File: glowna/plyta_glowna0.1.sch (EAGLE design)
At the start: 217 parts, among them IC1 4504D, IC2 MAX481CSA, IC3 4504D, IC4 OPA4658UU, Q1 CSM-7X-DU, Q2 N-HEXFET-2D_SOT232-IRLL014N, Q3 N-HEXFET-2D_SOT232-IRLL014N, Q4 N-HEXFET-2D_SOT232-IRLL014N, Q5 N-HEXFET-2D_SOT232-IRLL014N, Q6 N-HEXFET-2D_SOT232-IRLL014N, X1 MINI-USB_SHIELD5P2-32005-601

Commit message: a
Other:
- note removed: "może jakiś elektrolit ?"
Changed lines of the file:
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@@
 <?xml version="1.0" encoding="utf-8"?>
 <!DOCTYPE eagle SYSTEM "eagle.dtd">
-<eagle version="7.5.0">
+<eagle version="7.2.0">
 <drawing>
 <settings>
@@
 <text x="-43.18" y="91.44" size="5.08" layer="99">Jaki
 kwarc?</text>
-<text x="-139.7" y="71.12" size="1.27" layer="99">może jakiś elektrolit ?</text>
 <text x="157.48" y="-17.78" size="6.4516" layer="97">USB</text>
 <wire x1="434.34" y1="91.44" x2="500.38" y2="91.44" width="0.1524" layer="97" style="longdash"/>

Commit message: konczymy
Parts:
- added R65, R66, R67: (no value), rcl:R-EU_R2512
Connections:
- net N$77 renamed W1_1
- net N$83 renamed W2_1
- net N$85 renamed W3_1
- removed net N$78: R50.1
- removed net N$84: R58.1
- removed net N$86: R61.1
- new net W1_2: R50.1, R65.1, U$7.P$1, U$7.P$2
- new net W2_2: R58.1, R66.1, U$9.P$1, U$9.P$2
- new net W3_2: R61.1, R67.1, U$11.P$1, U$11.P$2
- net +24V: now also R65.2, R66.2, R67.2; no longer U$11.P$1, U$11.P$2, U$7.P$1, U$7.P$2, U$9.P$1, U$9.P$2
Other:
- note added: "może jakiś elektrolit ?"

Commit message: koniec?
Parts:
- added U$20, U$21, U$22: SEPARATOR, robione:SEPARATOR
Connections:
- net +24V: now also U$20.1, U$21.1, U$22.1
- net W1_1: now also U$20.2
- net W2_1: now also U$21.2
- net W3_1: now also U$22.2
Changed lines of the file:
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@@
 <part name="P+5" library="supply1" deviceset="+24V" device=""/>
 <part name="P+6" library="supply1" deviceset="+24V" device=""/>
+<part name="U$20" library="robione" deviceset="SEPARATOR" device=""/>
+<part name="U$21" library="robione" deviceset="SEPARATOR" device=""/>
+<part name="U$22" library="robione" deviceset="SEPARATOR" device=""/>
 </parts>
 <sheets>
@@
 <attribute name="VALUE" x="220.98" y="76.2" size="1.778" layer="96" rot="R180"/>
 </instance>
+<instance part="U$20" gate="G$1" x="226.06" y="119.38"/>
+<instance part="U$21" gate="G$1" x="223.52" y="93.98"/>
+<instance part="U$22" gate="G$1" x="223.52" y="68.58"/>
 </instances>
 <busses>
@@
 <wire x1="220.98" y1="119.38" x2="223.52" y2="119.38" width="0.1524" layer="91"/>
 <junction x="220.98" y="119.38"/>
+<pinref part="U$20" gate="G$1" pin="1"/>
 </segment>
 <segment>
@@
 <wire x1="220.98" y1="96.52" x2="220.98" y2="93.98" width="0.1524" layer="91"/>
 <pinref part="P+5" gate="1" pin="+24V"/>
-<wire x1="220.98" y1="93.98" x2="223.52" y2="93.98" width="0.1524" layer="91"/>
+<pinref part="U$21" gate="G$1" pin="1"/>
 <junction x="220.98" y="93.98"/>
-<label x="223.52" y="93.98" size="1.778" layer="95" xref="yes"/>
 </segment>
 <segment>
@@
 <wire x1="220.98" y1="68.58" x2="220.98" y2="71.12" width="0.1524" layer="91"/>
 <pinref part="P+6" gate="1" pin="+24V"/>
-<wire x1="220.98" y1="68.58" x2="223.52" y2="68.58" width="0.1524" layer="91"/>
+<pinref part="U$22" gate="G$1" pin="1"/>
 <junction x="220.98" y="68.58"/>
-<label x="223.52" y="68.58" size="1.778" layer="95" xref="yes"/>
 </segment>
 </net>
@@
 <label x="-170.18" y="2.54" size="1.6764" layer="95" rot="R180" xref="yes"/>
 </segment>
+<segment>
+<pinref part="U$20" gate="G$1" pin="2"/>
+<wire x1="228.6" y1="119.38" x2="231.14" y2="119.38" width="0.1524" layer="91"/>
+<label x="231.14" y="119.38" size="1.27" layer="95" xref="yes"/>
+</segment>
 </net>
 <net name="W1_2" class="0">
@@
 <label x="-177.8" y="-27.94" size="1.6764" layer="95" rot="R180" xref="yes"/>
 </segment>
+<segment>
+<pinref part="U$21" gate="G$1" pin="2"/>
+<wire x1="226.06" y1="93.98" x2="228.6" y2="93.98" width="0.1524" layer="91"/>
+<label x="228.6" y="93.98" size="1.27" layer="95" xref="yes"/>
+</segment>
 </net>
 <net name="W2_2" class="0">
@@
 <label x="-101.6" y="2.54" size="1.6764" layer="95" rot="R180" xref="yes"/>
 </segment>
+<segment>
+<pinref part="U$22" gate="G$1" pin="2"/>
+<wire x1="226.06" y1="68.58" x2="228.6" y2="68.58" width="0.1524" layer="91"/>
+<label x="228.6" y="68.58" size="1.27" layer="95" xref="yes"/>
+</segment>
 </net>

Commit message: to juz jest koniec
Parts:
- added U$23, U$24, U$25: SEPARATOR, robione:SEPARATOR
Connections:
- new net N$77: R65.2, U$23.2, U$8.P$1, U$8.P$2
- new net N$78: R66.1, U$10.P$1, U$10.P$2, U$24.2
- new net N$83: R67.1, U$12.P$1, U$12.P$2, U$25.2
- net +24V: now also U$11.P$1, U$11.P$2, U$7.P$1, U$7.P$2, U$9.P$1, U$9.P$2; no longer R65.2, R66.2, R67.2, U$20.1, U$21.1, U$22.1
- net GND: now also R65.1, R66.2, R67.2, U$20.1, U$21.1, U$22.1; no longer U$10.P$1, U$10.P$2, U$12.P$1, U$12.P$2, U$8.P$1, U$8.P$2
- net W1_1: now also U$23.1; no longer U$20.2
- net W1_2: now also U$20.2; no longer R65.1, U$7.P$1, U$7.P$2
- net W2_1: now also U$24.1; no longer U$21.2
- net W2_2: now also U$21.2; no longer R66.1, U$9.P$1, U$9.P$2
- net W3_1: now also U$25.1; no longer U$22.2
- net W3_2: now also U$22.2; no longer R67.1, U$11.P$1, U$11.P$2
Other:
- moved on the sheet: R65, R66, R67

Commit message: z mojej strony koniec
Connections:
- removed net GPIO_WENTYLATOR: U$1.PG2
- removed net N$22: IC1A.AI
- removed net N$23: JP25.3
- removed net N$24: JP25.2
- removed net N$25: IC1A.BI
- removed net N$27: JP26.1
- removed net N$28: IC1A.CI
- removed net N$29: JP26.8
- removed net N$30: IC1A.DI
- removed net N$31: IC1A.EI
- removed net N$32: IC1A.FI
- removed net TIM4_PWM_WENTYLATOR: U$1.PD15
- new net GPIO_WEN: IC1A.FI, U$1.PG2
- new net TIM4_PWM_WEN: IC1A.EI, U$1.PD15
- new net VDD: C22.+, D_1.C, D_2.C, D_3.C, D_4.C, F2.2, GRZALKA.2, GRZALKA1.2, GRZALKA2.2, GRZALKA3.2, TRANSIL_3.C
- net +24V: no longer C22.+, D_1.C, D_2.C, D_3.C, D_4.C, F2.2, GRZALKA.2, GRZALKA1.2, GRZALKA2.2, GRZALKA3.2, TRANSIL_3.C
- net GND: no longer JP26.6
- net GRZALKA1: now also IC1A.AI
- net GRZALKA2: now also IC1A.BI
- net GRZALKA3: now also IC1A.CI
- net GRZALKA4: now also IC1A.DI
- net I2C1_SCL: now also JP25.2
- net I2C1_SDA: now also JP25.3
- net UART4_WIFI_RX: now also JP26.1
- net UART4_WIFI_TX: now also JP26.8
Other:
- note added: "Odcinanie sterownika 12v"
- note added: "Pomiar pradu"
- note removed: "Miso & mosi dla pewności do sprawdzenia"
- moved on the sheet: C28

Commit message: zabezpieczenia
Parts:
- added D27, D28, D29, D30, D31, D32, D33, D34, D35, D36, D37, D38, D39: BAT54S, diode:BAT54S
- added R68, R69, R70, R71, R72, R73, R74, R75, R76, R77, R78, R79, R80: 5k, rcl:R-EU_R0603
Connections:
- new net N$22: D28.C1A2, JP17.1, R69.2
- new net N$23: JP7.1, R68.2
- new net N$24: D32.C1A2, JP19.1, R71.2
- new net N$25: D33.C1A2, JP18.1, R70.2
- new net N$27: D31.C1A2, JP20.1, R72.2
- new net N$28: D30.C1A2, JP22.1, R74.2
- new net N$29: D29.C1A2, JP21.1, R73.2
- new net N$32: JP24.1, R75.1
- new net N$84: JP24.3, R76.1
- new net N$85: JP24.5, R77.1
- new net N$86: JP24.7, R78.1
- new net N$87: JP24.9, R79.1
- new net N$88: JP24.11, R80.1
- net +3V3: now also D27.C2, D28.C2, D29.C2, D30.C2, D31.C2, D32.C2, D33.C2, D34.C2, D35.C2, D36.C2, D37.C2, D38.C2, D39.C2
- net ENDSTOP1: now also D36.C1A2, R78.2; no longer JP24.7
- net ENDSTOP2: now also D35.C1A2, R79.2; no longer JP24.9
- net ENDSTOP3: now also D34.C1A2, R80.2; no longer JP24.11
- net ENDSTOP_E1: now also D39.C1A2, R75.2; no longer JP24.1
- net ENDSTOP_E2: now also D38.C1A2, R76.2; no longer JP24.3
- net ENDSTOP_E3: now also D37.C1A2, R77.2; no longer JP24.5
- net ENDSTOP_X_MAX: now also R69.1; no longer JP17.1
- net ENDSTOP_X_MINI: now also R70.1; no longer JP18.1
- net ENDSTOP_Y_MAX: now also R71.1; no longer JP19.1
- net ENDSTOP_Y_MINI: now also R72.1; no longer JP20.1
- net ENDSTOP_Z_MAX: now also R73.1; no longer JP21.1
- net ENDSTOP_Z_MINI: now also R74.1; no longer JP22.1
- net GND: now also D27.A1, D28.A1, D29.A1, D30.A1, D31.A1, D32.A1, D33.A1, D34.A1, D35.A1, D36.A1, D37.A1, D38.A1, D39.A1
- net PWM_SOFT_LASER: now also D27.C1A2, R68.1; no longer JP7.1
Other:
- moved on the sheet: JP24

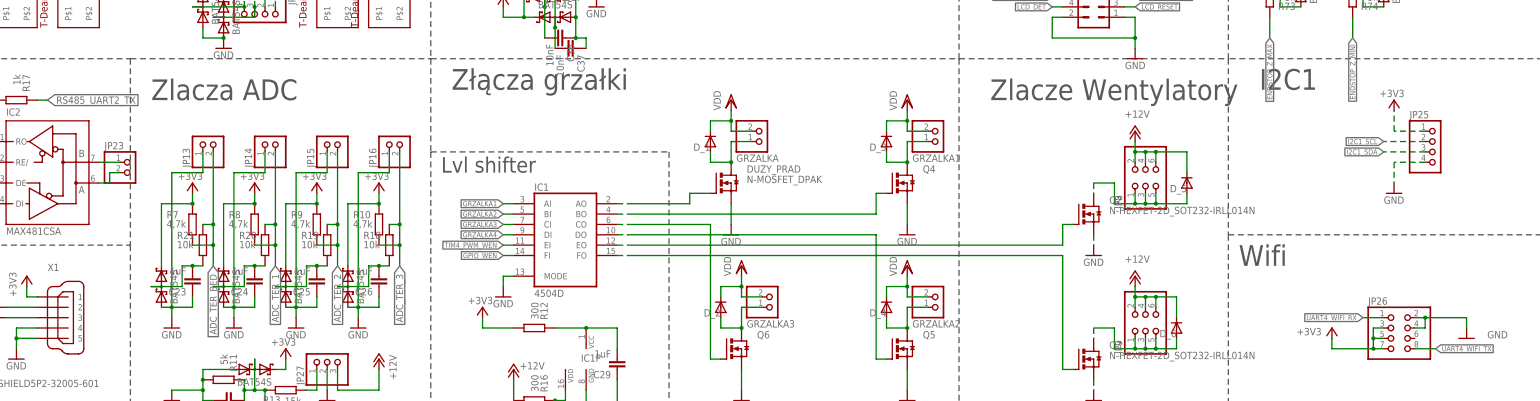
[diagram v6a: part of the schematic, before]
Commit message: rezystorki w i2c
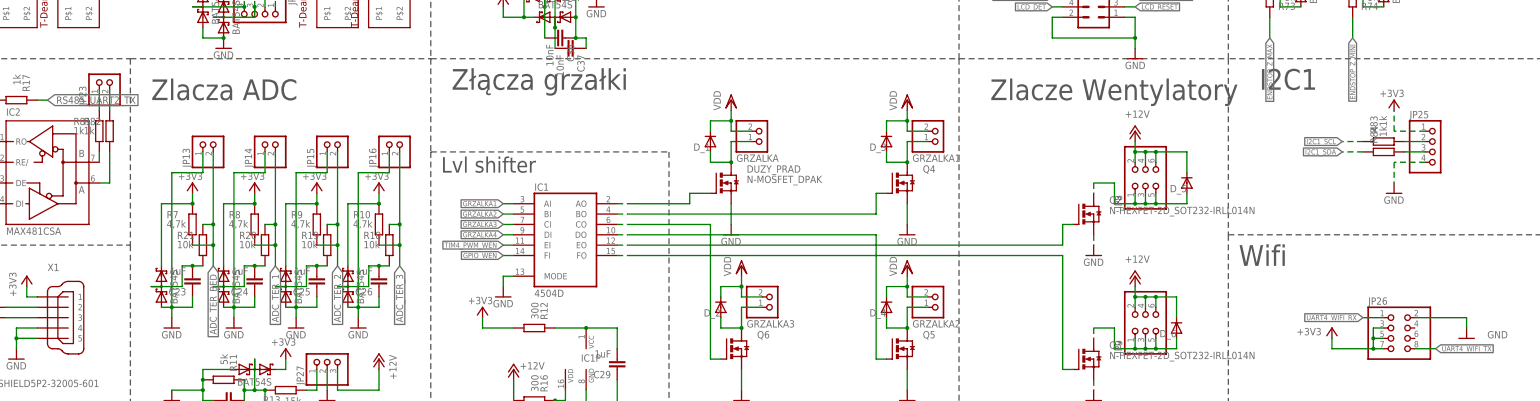
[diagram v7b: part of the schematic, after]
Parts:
- added R81, R82, R83, R84: 1k, rcl:R-EU_R0603
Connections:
- new net N$30: IC2G$1.B, R81.2
- new net N$31: IC2G$1.A, R82.2
- new net N$89: JP25.2, R83.2
- new net N$90: JP25.3, R84.2
- net GND: no longer JP26.4
- net I2C1_SCL: now also R83.1; no longer JP25.2
- net I2C1_SDA: now also R84.1; no longer JP25.3
- net N$66: now also R81.1; no longer IC2G$1.B
- net N$82: now also R82.1; no longer IC2G$1.A
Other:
- note removed: "może jakiś elektrolit ?"
- moved on the sheet: JP23
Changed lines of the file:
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@@
 <part name="+3V47" library="supply1" deviceset="+3V3" device=""/>
 <part name="GND78" library="supply1" deviceset="GND" device=""/>
+<part name="R81" library="rcl" deviceset="R-EU_" device="R0603" value="1k"/>
+<part name="R82" library="rcl" deviceset="R-EU_" device="R0603" value="1k"/>
+<part name="R83" library="rcl" deviceset="R-EU_" device="R0603" value="1k"/>
+<part name="R84" library="rcl" deviceset="R-EU_" device="R0603" value="1k"/>
 </parts>
 <sheets>
@@
 <text x="-43.18" y="91.44" size="5.08" layer="99">Jaki
 kwarc?</text>
-<text x="-139.7" y="71.12" size="1.27" layer="99">może jakiś elektrolit ?</text>
 <text x="157.48" y="-17.78" size="6.4516" layer="97">USB</text>
 <wire x1="434.34" y1="91.44" x2="500.38" y2="91.44" width="0.1524" layer="97" style="longdash"/>
@@
 <attribute name="VALUE" x="-87.884" y="40.259" size="1.778" layer="96" rot="R180"/>
 </instance>
-<instance part="JP23" gate="G$1" x="231.14" y="12.7"/>
+<instance part="JP23" gate="G$1" x="226.06" y="35.56" rot="R90"/>
 <instance part="R65" gate="G$1" x="223.52" y="116.84" rot="R180"/>
 <instance part="R66" gate="G$1" x="223.52" y="91.44"/>
@@
 </instance>
 <instance part="GND78" gate="1" x="553.72" y="63.5"/>
+<instance part="R81" gate="G$1" x="223.52" y="22.86" smashed="yes" rot="R270">
+<attribute name="NAME" x="217.17" y="24.3586" size="1.778" layer="95"/>
+<attribute name="VALUE" x="217.17" y="22.098" size="1.778" layer="96"/>
+</instance>
+<instance part="R82" gate="G$1" x="226.06" y="22.86" smashed="yes" rot="R270">
+<attribute name="NAME" x="219.71" y="24.3586" size="1.778" layer="95"/>
+<attribute name="VALUE" x="219.71" y="22.098" size="1.778" layer="96"/>
+</instance>
+<instance part="R83" gate="G$1" x="538.48" y="20.32" smashed="yes" rot="MR180">
+<attribute name="NAME" x="536.9814" y="26.67" size="1.778" layer="95" rot="MR270"/>
+<attribute name="VALUE" x="539.242" y="26.67" size="1.778" layer="96" rot="MR270"/>
+</instance>
+<instance part="R84" gate="G$1" x="538.48" y="17.78" smashed="yes" rot="MR180">
+<attribute name="NAME" x="536.9814" y="24.13" size="1.778" layer="95" rot="MR270"/>
+<attribute name="VALUE" x="539.242" y="24.13" size="1.778" layer="96" rot="MR270"/>
+</instance>
 </instances>
 <busses>
@@
 <segment>
 <pinref part="JP26" gate="A" pin="2"/>
-<wire x1="546.1" y1="-22.86" x2="548.64" y2="-22.86" width="0.1524" layer="91"/>
-<wire x1="548.64" y1="-22.86" x2="558.8" y2="-22.86" width="0.1524" layer="91"/>
+<wire x1="546.1" y1="-22.86" x2="558.8" y2="-22.86" width="0.1524" layer="91"/>
 <wire x1="558.8" y1="-22.86" x2="558.8" y2="-25.4" width="0.1524" layer="91"/>
-<pinref part="JP26" gate="A" pin="4"/>
-<wire x1="546.1" y1="-25.4" x2="548.64" y2="-25.4" width="0.1524" layer="91"/>
-<wire x1="548.64" y1="-25.4" x2="548.64" y2="-22.86" width="0.1524" layer="91"/>
-<junction x="548.64" y="-22.86"/>
 <pinref part="GND63" gate="1" pin="GND"/>
 </segment>
@@
 </segment>
 <segment>
-<pinref part="JP25" gate="A" pin="3"/>
-<wire x1="548.64" y1="17.78" x2="538.48" y2="17.78" width="0.1524" layer="91" style="longdash"/>
-<label x="538.48" y="17.78" size="1.27" layer="95" rot="R180" xref="yes"/>
+<label x="528.32" y="17.78" size="1.27" layer="95" rot="R180" xref="yes"/>
+<pinref part="R84" gate="G$1" pin="1"/>
+<wire x1="533.4" y1="17.78" x2="528.32" y2="17.78" width="0.1524" layer="91" style="longdash"/>
 </segment>
 </net>
@@
 </segment>
 <segment>
-<pinref part="JP25" gate="A" pin="2"/>
-<wire x1="548.64" y1="20.32" x2="538.48" y2="20.32" width="0.1524" layer="91" style="longdash"/>
-<label x="538.48" y="20.32" size="1.27" layer="95" rot="R180" xref="yes"/>
+<label x="528.32" y="20.32" size="1.27" layer="95" rot="R180" xref="yes"/>
+<pinref part="R83" gate="G$1" pin="1"/>
+<wire x1="533.4" y1="20.32" x2="528.32" y2="20.32" width="0.1524" layer="91" style="longdash"/>
 </segment>
 </net>
@@
 </segment>
 </net>
-<net name="N$66" class="0">
-<segment>
-<pinref part="IC2" gate="G$1" pin="B"/>
-<pinref part="JP23" gate="G$1" pin="1"/>
-<wire x1="223.52" y1="15.24" x2="228.6" y2="15.24" width="0.1524" layer="91"/>
-</segment>
-</net>
-<net name="N$82" class="0">
-<segment>
-<pinref part="IC2" gate="G$1" pin="A"/>
-<wire x1="223.52" y1="10.16" x2="226.06" y2="10.16" width="0.1524" layer="91"/>
-<wire x1="226.06" y1="10.16" x2="226.06" y2="12.7" width="0.1524" layer="91"/>
-<pinref part="JP23" gate="G$1" pin="2"/>
-<wire x1="226.06" y1="12.7" x2="228.6" y2="12.7" width="0.1524" layer="91"/>
-</segment>
-</net>
 <net name="N$77" class="0">
 <segment>
@@
 </segment>
 </net>
+<net name="N$30" class="0">
+<segment>
+<pinref part="IC2" gate="G$1" pin="B"/>
+<pinref part="R81" gate="G$1" pin="2"/>
+<wire x1="223.52" y1="15.24" x2="223.52" y2="17.78" width="0.1524" layer="91"/>
+</segment>
+</net>
+<net name="N$31" class="0">
+<segment>
+<pinref part="IC2" gate="G$1" pin="A"/>
+<wire x1="223.52" y1="10.16" x2="226.06" y2="10.16" width="0.1524" layer="91"/>
+<pinref part="R82" gate="G$1" pin="2"/>
+<wire x1="226.06" y1="10.16" x2="226.06" y2="17.78" width="0.1524" layer="91"/>
+</segment>
+</net>
+<net name="N$66" class="0">
+<segment>
+<pinref part="R81" gate="G$1" pin="1"/>
+<pinref part="JP23" gate="G$1" pin="1"/>
+<wire x1="223.52" y1="27.94" x2="223.52" y2="33.02" width="0.1524" layer="91"/>
+</segment>
+</net>
+<net name="N$82" class="0">
+<segment>
+<pinref part="R82" gate="G$1" pin="1"/>
+<pinref part="JP23" gate="G$1" pin="2"/>
+<wire x1="226.06" y1="27.94" x2="226.06" y2="33.02" width="0.1524" layer="91"/>
+</segment>
+</net>
+<net name="N$89" class="0">
+<segment>
+<pinref part="R83" gate="G$1" pin="2"/>
+<pinref part="JP25" gate="A" pin="2"/>
+<wire x1="543.56" y1="20.32" x2="548.64" y2="20.32" width="0.1524" layer="91"/>
+</segment>
+</net>
+<net name="N$90" class="0">
+<segment>
+<pinref part="R84" gate="G$1" pin="2"/>
+<pinref part="JP25" gate="A" pin="3"/>
+<wire x1="543.56" y1="17.78" x2="548.64" y2="17.78" width="0.1524" layer="91"/>
+</segment>
+</net>

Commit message: wstepny schemat
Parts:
- removed D1, D10, D11, D12, D13, D14, D15, D16, D17, D18, D19, D2, D20, D27, D28, D29, D3, D30, D31, D32, D33, D34, D35, D36, D37, D38, D39, D4, D5, D6, D7, D8, D9: BAT54S, diode:BAT54S
- removed D_1, D_2, D_3, D_4: (no value), diode:DIODE-DO-214AC
- removed Q4, Q5, Q6: N-HEXFET-2D_SOT232-IRLL014N, transistor-power:N-HEXFET-2D_SOT232-IRLL014N
- removed X1: MINI-USB_SHIELD5P2-32005-601, con-cypressindustries:MINI-USB_SHIELD5P2-32005-601
- added DUZY_PRAD1, DUZY_PRAD2, DUZY_PRAD3: N-MOSFET_DPAK, transistor-power:N-MOSFET_DPAK
- added LED1: (no value), led:LEDSML0603
- added R85: 1k, rcl:R-EU_R0603
- added R86, R87, R88, R89, R90, R91: 500, rcl:R-EU_R0603
- added R92: 470, rcl:R-EU_R0603
- R19: value 10k -> 4,7k
- R68: value 5k -> 500
- R83, R84: value 1k -> 5k
- R9: value 4,7k -> 10k
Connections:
- new net LCD_RS: SV1.4
- new net N$91: JP18.3, R86.2
- new net N$92: JP19.3, R88.2
- new net N$93: JP20.3, R89.2
- new net N$94: JP21.3, R90.2
- new net N$95: JP22.3, R91.2
- new net N$96: C27.1, R11.1, R13.1
- new net N$97: LED1.A, R92.2
- net +3V3: now also R19.1, R68.2, R83.2, R84.2, R86.1, R87.1, R88.1, R89.1, R90.1, R91.1, R92.1; no longer D1.C2, D10.C2, D11.C2, D12.C2, D13.C2, D14.C2, D15.C2, D16.C2, D17.C2, D18.C2, D19.C2, D2.C2, D20.C2, D27.C2, D28.C2, D29.C2, D3.C2, D30.C2, D31.C2, D32.C2, D33.C2, D34.C2, D35.C2, D36.C2, D37.C2, D38.C2, D39.C2, D4.C2, D5.C2, D6.C2, D7.C2, D8.C2, D9.C2, JP17.3, JP18.3, JP19.3, JP20.3, JP21.3, JP22.3, JP24.10, JP24.12, JP24.2, JP24.4, JP24.6, JP24.8, R9.1, X1G41.1
- net ADC3_CZUJNIK_INDUKCYJNY: no longer C27.1, D8.C1A2, R11.1, R13.1
- net ADC_TER_1: no longer JP14.2, R20.1, R8.2
- net ADC_TER_2: no longer JP15.2, R19.1, R9.2
- net ADC_TER_3: no longer JP16.2, R10.2, R18.1
- net ADC_TER_BED: now also C23.2, C24.2, C25.2, C26.2, R18.2, R20.2, R21.2, R9.2; no longer R21.1, R7.2
- net ENDSTOP1: no longer D36.C1A2
- net ENDSTOP2: no longer D35.C1A2
- net ENDSTOP3: no longer D34.C1A2
- net ENDSTOP_E1: no longer D39.C1A2
- net ENDSTOP_E2: no longer D38.C1A2
- net ENDSTOP_E3: no longer D37.C1A2
- net GND: now also DUZY_PRAD1.S, DUZY_PRAD2.S, DUZY_PRAD3.S, JP13.1, LED1.C; no longer D1.A1, D10.A1, D11.A1, D12.A1, D13.A1, D14.A1, D15.A1, D16.A1, D17.A1, D18.A1, D19.A1, D2.A1, D20.A1, D27.A1, D28.A1, D29.A1, D3.A1, D30.A1, D31.A1, D32.A1, D33.A1, D34.A1, D35.A1, D36.A1, D37.A1, D38.A1, D39.A1, D4.A1, D5.A1, D6.A1, D7.A1, D8.A1, D9.A1, Q4.S, Q5.S, Q6.S, X1G41.4, X1G41.5
- net I2C1_SCL: now also JP25.2
- net I2C1_SDA: now also JP25.3
- net LCD_RW: no longer SV1.4
- net N$12: no longer D_1.A
- net N$13: no longer X1G41.2
- net N$14: no longer X1G41.3
- net N$17: now also DUZY_PRAD1.D; no longer D_3.A, Q4.D
- net N$18: now also DUZY_PRAD2.D; no longer D_4.A, Q5.D
- net N$20: now also DUZY_PRAD3.D; no longer D_2.A, Q6.D
- net N$22: no longer D28.C1A2
- net N$23: now also R85.1; no longer R68.2
- net N$24: no longer D32.C1A2
- net N$25: no longer D33.C1A2
- net N$27: no longer D31.C1A2
- net N$28: no longer D30.C1A2
- net N$29: no longer D29.C1A2
- net N$33: now also DUZY_PRAD1.G; no longer Q4.G
- net N$34: now also DUZY_PRAD3.G; no longer Q6.G
- net N$35: now also DUZY_PRAD2.G; no longer Q5.G
- net N$41: no longer D5.C1A2
- net N$42: now also JP14.2, R8.2, R9.1; no longer C25.2, D3.C1A2, R19.2
- net N$43: now also JP13.2, R21.1, R7.2; no longer C24.2, D2.C1A2, R20.2
- net N$44: now also JP15.2, R10.2, R18.1; no longer C26.2, D4.C1A2, R18.2
- net N$45: no longer D6.C1A2
- net N$46: no longer D7.C1A2
- net N$47: now also JP16.2, R19.2, R20.1; no longer C23.2, D1.C1A2, R21.2
- net N$48: no longer D16.C1A2
- net N$49: no longer D9.C1A2
- net N$50: no longer D10.C1A2
- net N$51: no longer D15.C1A2
- net N$52: no longer D12.C1A2
- net N$53: no longer D13.C1A2
- net N$55: no longer D18.C1A2
- net N$56: no longer D17.C1A2
- net N$57: no longer D11.C1A2
- net N$58: no longer D20.C1A2
- net N$59: no longer D19.C1A2
- net N$89: now also JP24.10, JP24.12, JP24.2, JP24.4, JP24.6, JP24.8, R68.1; no longer JP25.2, R83.2
- net N$90: now also JP17.3, R87.2; no longer JP25.3, R84.2
- net PWM_SOFT_LASER: now also R85.2; no longer D27.C1A2, R68.1
- net TIM8_PWM_Z1: no longer D14.C1A2
- net VDD: no longer D_1.C, D_2.C, D_3.C, D_4.C
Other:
- note added: "Enkodery 5v? Stm wytrzyma?"
- note added: "Rezystory rs485"
- note added: "USB B"
- note removed: "1 ma mosfet dpak, pozostale 3 sot223"
- note removed: "<-- To coś chcę wyłączać"
- moved on the sheet: C15, C23, C24, C25, C26, C27, JP13, JP14, JP15, JP16, R10, R11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
